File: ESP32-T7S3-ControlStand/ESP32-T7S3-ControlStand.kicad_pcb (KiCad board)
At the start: 2 copper layers, 199.4 x 126.4 mm, 188 parts, among them IC601 USBLC6-2SC6, J1 Button & LED Panel, J10 RJ45, J101 Keypad Panel, J11 Barrel_Jack, J12 Battery, J2 Button & LED Panel, J3 STEMMA (Display), J4 Horn, J5 Brake, J6 Light Switch, J601 GCT_USB4105, J7 Reverser, J8 Throttle, J9 RJ45, P1 CONN_8, P2 Misc buttons, bell, status LED, P6 CONN_3, P7 CONN_3, P701 CONN_5, P8 CONN_5, P9 CONN_5, SW1 A, SW10 SW_PUSH_SMALL, SW11 SW_PUSH_SMALL, SW12 SW_PUSH_SMALL, SW13 SW_PUSH_SMALL, SW14 SW_PUSH_SMALL, SW15 SW_PUSH_SMALL, SW16 SW_PUSH_SMALL, SW17 SW_PUSH_SMALL, SW18 SW_PUSH_SMALL, SW19 SW_PUSH_SMALL, SW2 B, SW20 SW_PUSH_SMALL, SW21 SW_PUSH_SMALL, SW22 SW_PUSH_SMALL, SW23 On/Off, SW24 RESET, SW3 C, SW4 D, SW5 Bell, SW601 BOOT, SW7 SW_PUSH_SMALL, SW701 "1", SW702 "4", SW703 "7", SW704 "*", SW705 "2", SW706 "5", SW707 "8", SW708 "0", SW709 "3", SW710 "6", SW711 "9", SW712 "#", SW8 SW_PUSH_SMALL, SW9 SW_PUSH_SMALL, T1 Buttons, T2 LEDS, T3 Buttons, T4 LEDS, T5 + 15 in -, T6 + 15 out -, U1 MCP23017, U2 TBD62083A, U3 MCP23017, U4 TBD62083A, U5 TCAN332DR, U6 MCP73871, U601 ESP32_S3_WROOM-1, U7 LM2574HVM-5.0, U701 TCA8418, U8 TC1263-3.3VOATR

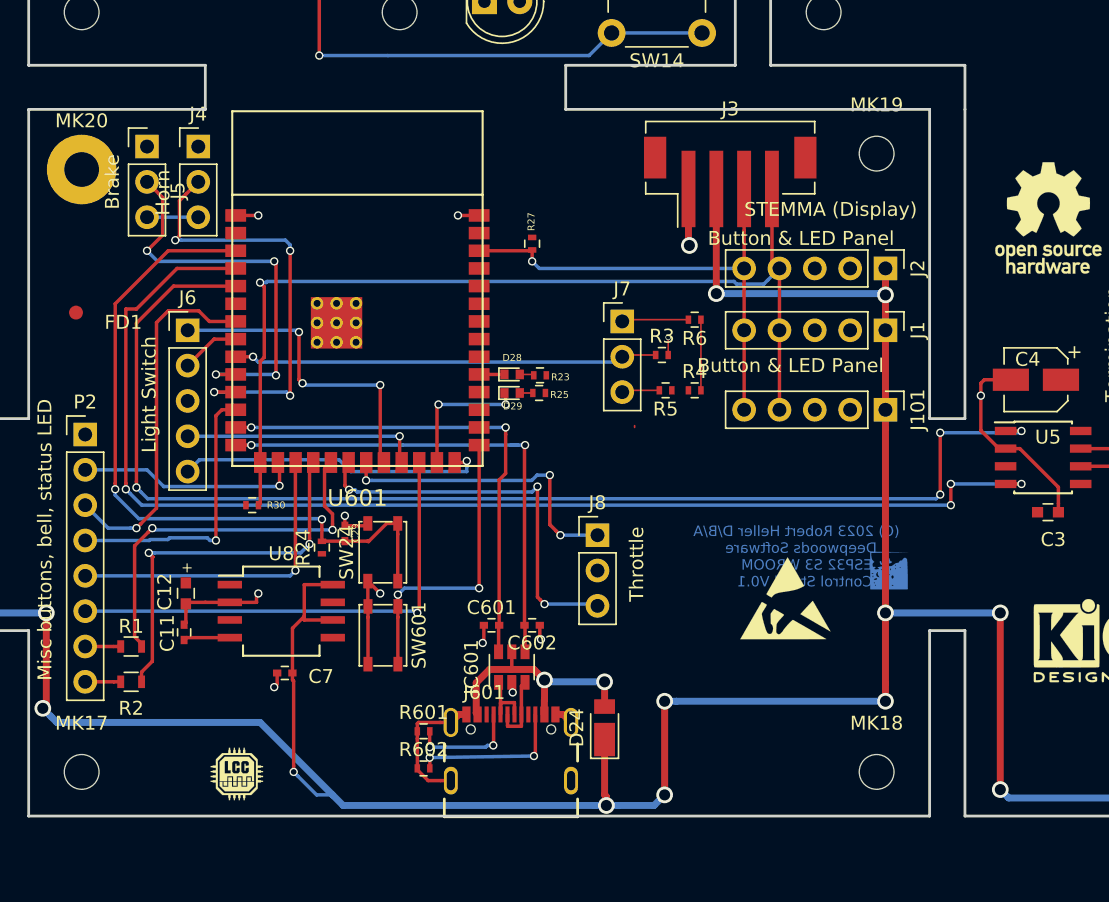
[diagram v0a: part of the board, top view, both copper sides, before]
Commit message: Add ESP32-T7S3-ControlStand.
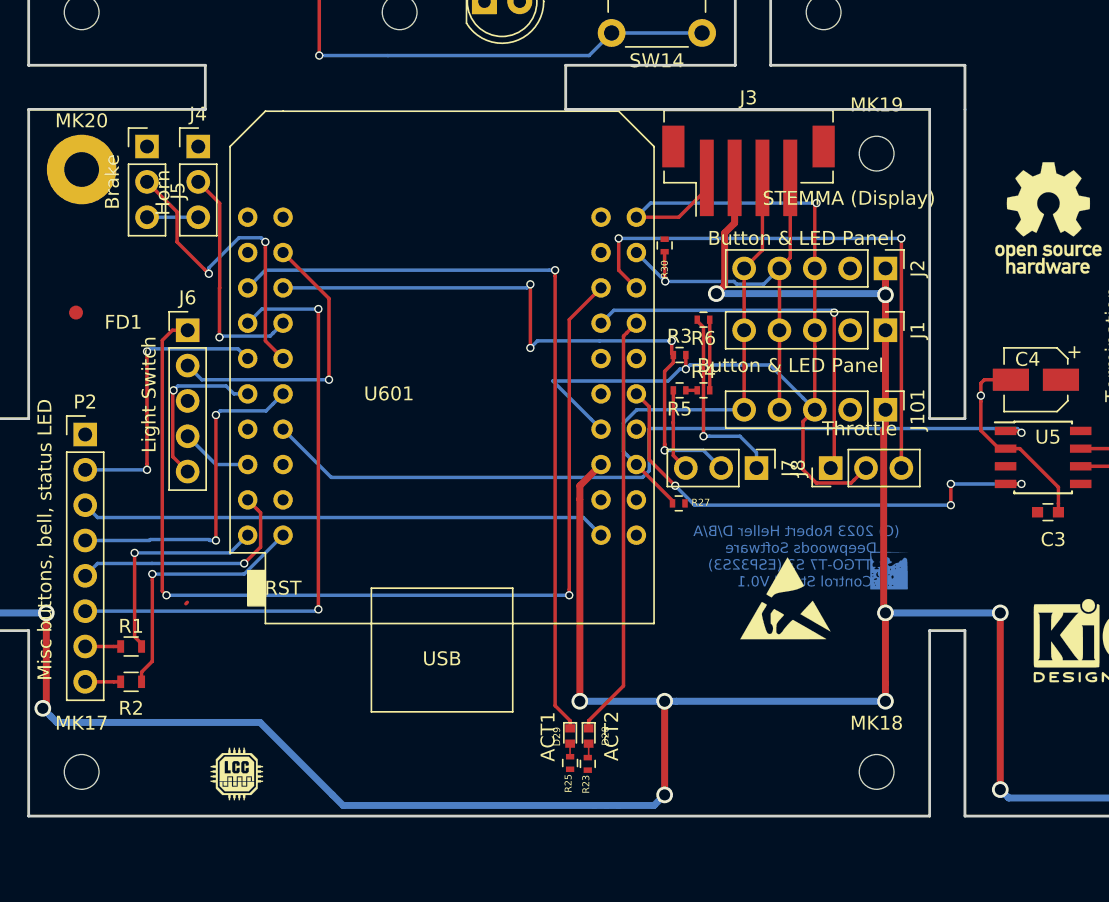
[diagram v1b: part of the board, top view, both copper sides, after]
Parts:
- removed C11: 470pf, Capacitors_SMD:C_0402
- removed C12: 1uf, MyCaps:C_0603_POL
- removed C29: 1uf, Capacitors_SMD:C_0402
- removed C601, C602: 22pf, Capacitors_SMD:C_0402
- removed C7: .1uf, Capacitors_SMD:C_0402
- removed D24: DFLS240-7, Diodes_SMD:D_PowerDI-123
- removed IC601: USBLC6-2SC6, TO_SOT_Packages_SMD:SOT-23-6
- removed J601: GCT_USB4105, GCT_USB:GCT_USB4105-GF-A
- removed R24: 10K, Resistors_SMD:R_0402
- removed R601, R602: 5.1K, Resistors_SMD:R_0402
- removed SW24: RESET, Buttons_Switches_SMD:SW_SPST_PTS810
- removed SW601: BOOT, Buttons_Switches_SMD:SW_SPST_PTS810
- removed U8: TC1263-3.3VOATR, Housings_SOIC:SO-8_5.3x6.2mm_Pitch1.27mm
- U601: value ESP32_S3_WROOM-1 -> TTGO-T7_S3-V1.1; footprint ESP32-WROOM:ESP32_S3_WROOM-1 -> ESP32_mini:ESP32_mini
- moved R30 35.0 mm to (158.8, 110.7), turned to 90 degrees
- moved R23 28.1 mm to (153.2, 148.0), turned to 90 degrees
- moved R25 26.7 mm to (152.0, 147.9), turned to 90 degrees
- moved D28 26.6 mm to (153.3, 146.0), turned to 270 degrees
- moved D29 25.0 mm to (152.0, 146.0), turned to 270 degrees
- moved R27 21.4 mm to (159.8, 129.3), turned to 180 degrees
- moved J8 17.4 mm to (170.7, 126.7), turned to 90 degrees
- moved J7 14.3 mm to (165.4, 126.7), turned to 270 degrees
- moved U601 6.64 mm to (142.7, 120.1)
- moved J3 1.54 mm to (164.8, 104.8)
- moved R3 1.27 mm to (159.8, 118.6)
- moved R5 1.01 mm to (159.8, 121.2)
- moved R4 0.64 mm to (161.5, 121.2)
- moved R6 0.64 mm to (161.5, 116.1)
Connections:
- MK20 pad 1: Net-(MK20-Pad1) -> GND
- R30 pad 2: +3V3 -> Net-(R30-Pad2)
- U601 pad 11: /Horn -> /L_Ditch
- U601 pad 13: /Processor Section/D- -> Net-(U601-Pad13)
- U601 pad 14: /Processor Section/D+ -> /CAN_TX
- U601 pad 15: /SCL -> /L_Bright
- U601 pad 16: /Button_A -> +3V3
- U601 pad 18: /Status_R -> Net-(U601-Pad18)
- U601 pad 2: +3V3 -> /RST
- U601 pad 20: /ThrottleA -> /Status_R
- U601 pad 21: /ThrottleB -> Net-(U601-Pad21)
- U601 pad 22: /L_Off -> GND
- U601 pad 23: /L_Bright -> Net-(U601-Pad23)
- U601 pad 24: /Bell -> /SCL
- U601 pad 25: /Processor Section/IO48(Act1) -> /L_Off
- U601 pad 26: /L_Ditch -> /ThrottleA
- U601 pad 27: Net-(SW601-Pad1) -> /ThrottleB
- U601 pad 28: Net-(U601-Pad28) -> /Processor Section/IO38(Act2)
- U601 pad 3: /RST -> Net-(U601-Pad3)
- U601 pad 31: /Processor Section/IO38(Act2) -> Net-(U601-Pad31)
- U601 pad 32: Net-(U601-Pad32) -> /CAN_RX
- U601 pad 33: Net-(U601-Pad33) -> GND
- U601 pad 35: Net-(U601-Pad35) -> +5V
- U601 pad 36: Net-(U601-Pad36) -> /SDA
- U601 pad 38: /SDA -> Net-(U601-Pad38)
- U601 pad 39: Net-(U601-Pad39) -> /Button_B
- U601 pad 4: /CAN_RX -> /L_Dim
- U601 pad 40: GND -> Net-(U601-Pad40)
- U601 pad 5: /CAN_TX -> /Processor Section/IO48(Act1)
- U601 pad 6: Net-(U601-Pad6) -> /Reverser
- U601 pad 7: /Button_B -> /Bell
- U601 pad 8: /L_Dim -> /Horn
- U601 pad 9: /Reverser -> /Button_A
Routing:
- net /CAN_RX: track 90.1 -> 36.4 mm
- net /RST: track 51.3 -> 0.00 mm, vias 2 -> 0
- net /L_Off: track 23.2 -> 72.6 mm, vias 3 -> 2
- net /Processor Section/IO48(Act1): track 9.90 -> 56.0 mm, vias 2 -> 1
- net /SCL: track 70.3 -> 31.6 mm
- net /Processor Section/D+: track 36.3 -> 0.00 mm, vias 2 -> 0
- net /Processor Section/D-: track 35.7 -> 0.00 mm, vias 2 -> 0
- net /CAN_TX: track 90.3 -> 59.6 mm, vias 4 -> 1
- net GND: track 279.0 -> 309.0 mm, vias 56 -> 47
- net /Processor Section/IO38(Act2): track 1.82 -> 30.5 mm
- net Net-(SW601-Pad1): track 21.3 -> 0.00 mm, vias 2 -> 0
- net VBUS: track 17.9 -> 0.00 mm, vias 2 -> 0
- net /L_Dim: track 4.24 -> 21.1 mm, vias 0 -> 1
- net /Reverser: track 30.4 -> 46.1 mm, vias 1 -> 4
- net /Horn: track 31.4 -> 17.0 mm, vias 4 -> 1
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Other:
- board text added: "(C) 2023 Robert Heller D/B/A Deepwoods Software TTGO-T7 S3 (ESP32S3) Control Stand V0.1"
- board text removed: "(C) 2023 Robert Heller D/B/A Deepwoods Software ESP32 S3 WROOM Control Stand V0.1"

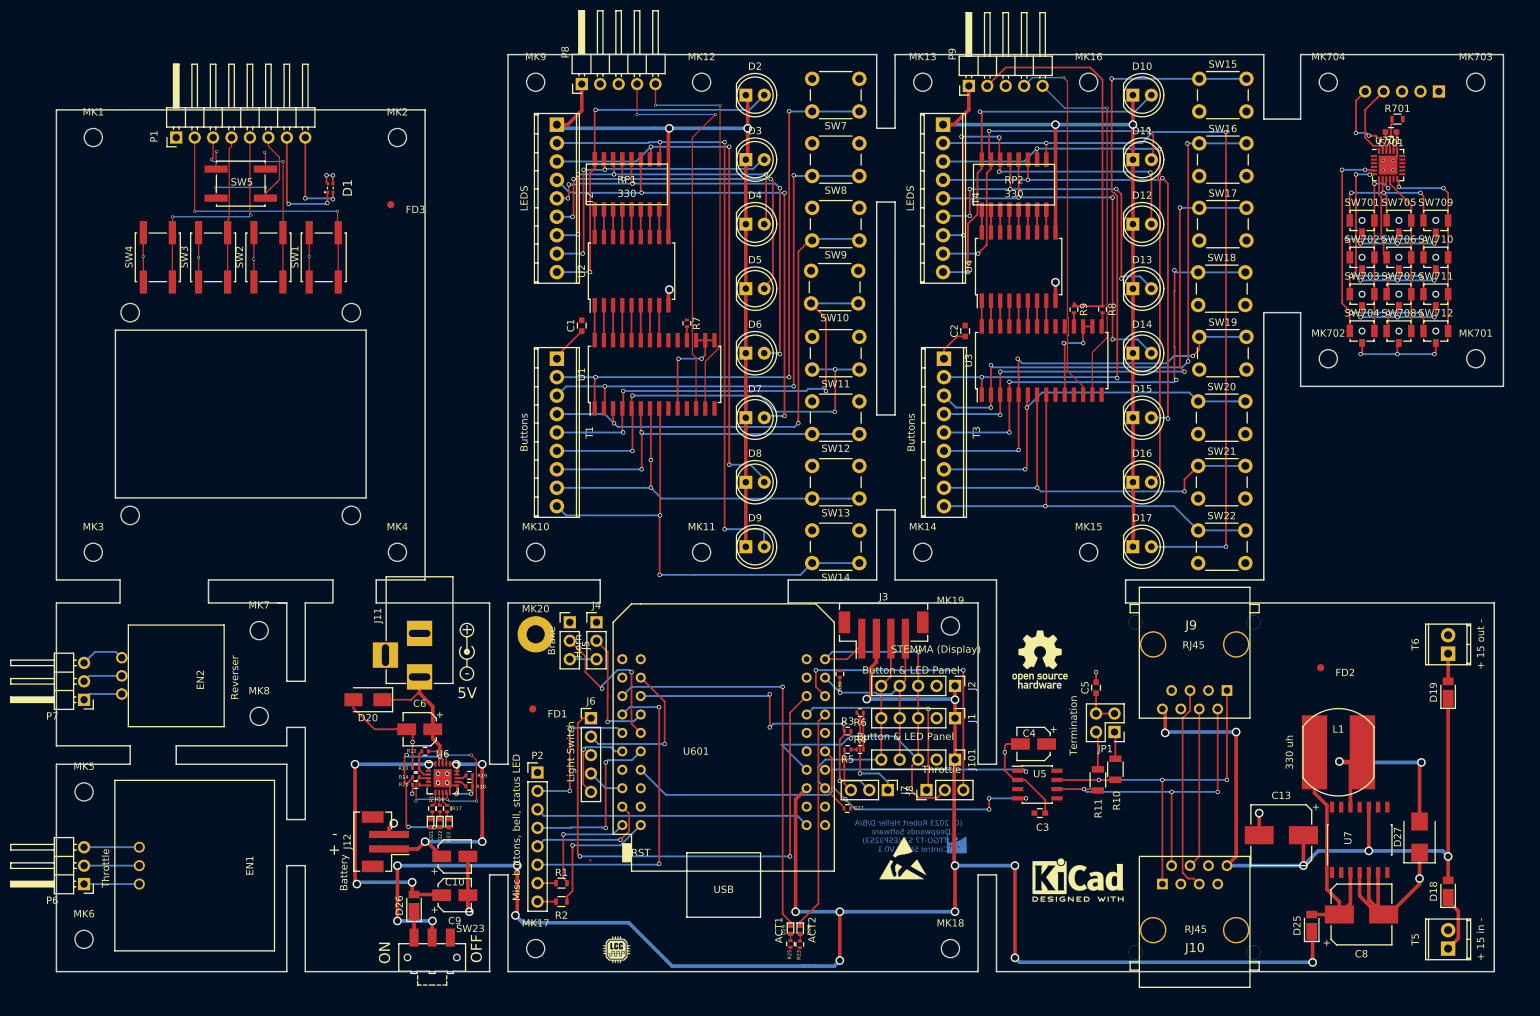
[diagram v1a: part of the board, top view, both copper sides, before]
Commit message: update ESP32-T7S3-ControlStand: Kicad 6, fix SDA, clean up and finalize PCB.
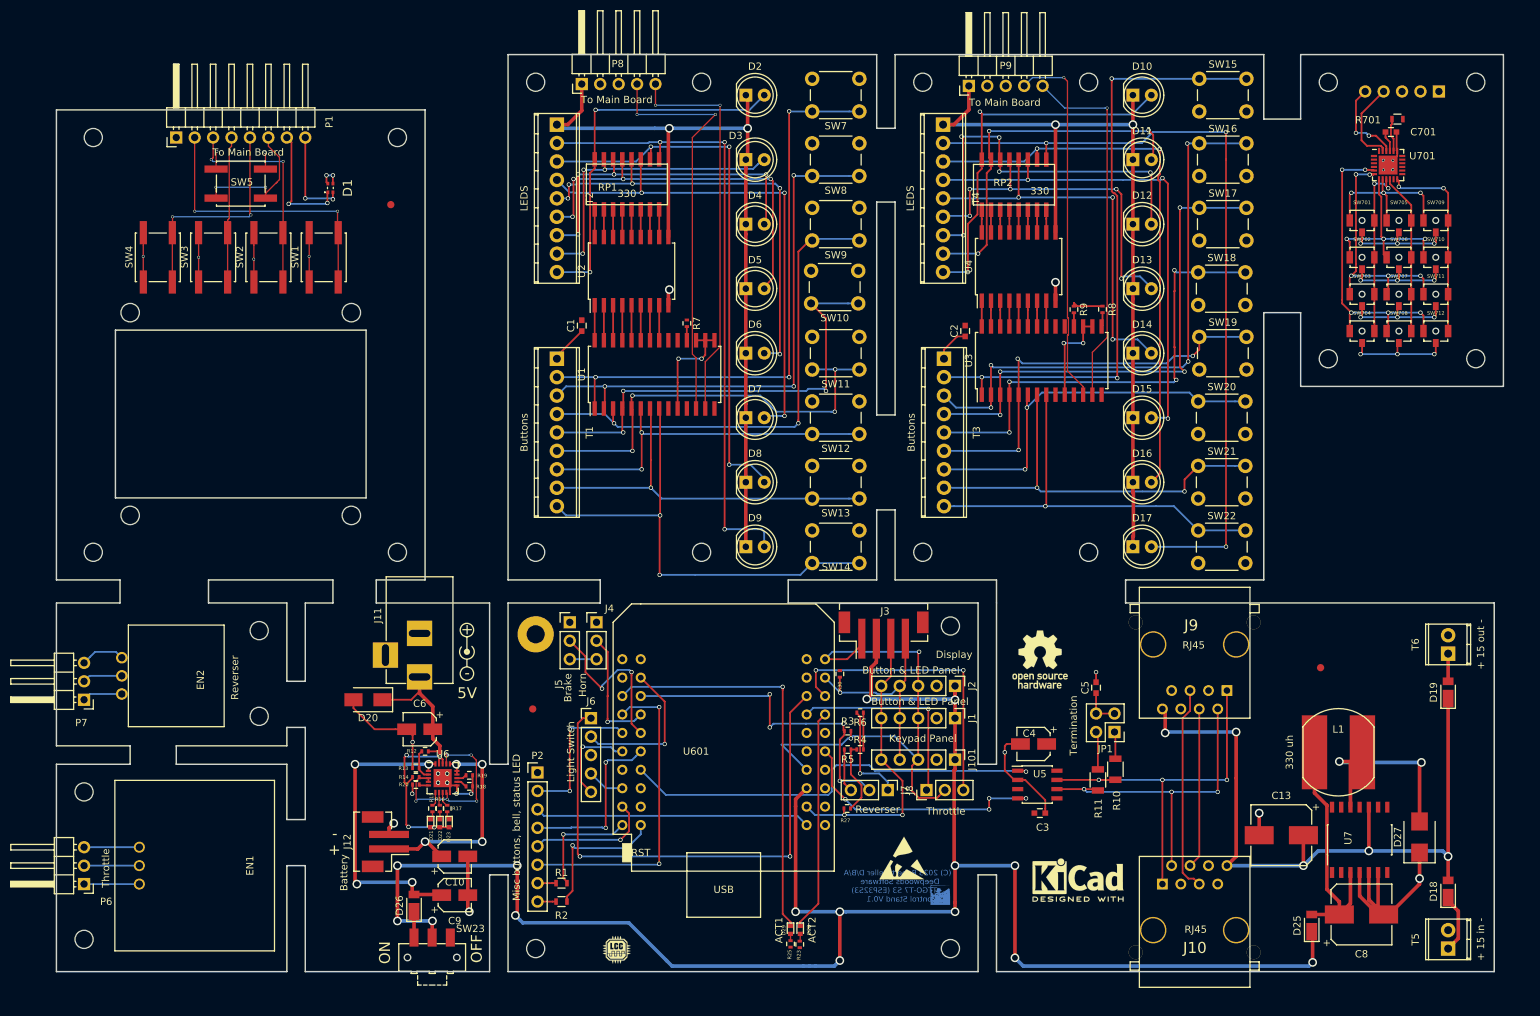
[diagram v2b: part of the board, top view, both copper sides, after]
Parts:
- J3: value STEMMA (Display) -> Display
- P1: value CONN_8 -> To Main Board
- P6, P7: value CONN_3 -> To Main Board
- P701, P8, P9: value CONN_5 -> To Main Board
- moved ? 7.47 mm to (172.6, 141.2)
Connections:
- J11 pad 3: Net-(J11-Pad3) -> unconnected-(J11-Pad3)
- P701 pad 1: Net-(P701-Pad1) -> unconnected-(P701-Pad1)
- R30 pad 2: Net-(R30-Pad2) -> unconnected-(R30-Pad2)
- SW23 pad 3: Net-(SW23-Pad3) -> unconnected-(SW23-Pad3)
- U1 pad 19: Net-(U1-Pad19) -> unconnected-(U1-Pad19)
- U1 pad 20: Net-(U1-Pad20) -> unconnected-(U1-Pad20)
- U3 pad 19: Net-(U3-Pad19) -> unconnected-(U3-Pad19)
- U3 pad 20: Net-(U3-Pad20) -> unconnected-(U3-Pad20)
- U5 pad 5: Net-(U5-Pad5) -> unconnected-(U5-Pad5)
- U5 pad 8: Net-(U5-Pad8) -> unconnected-(U5-Pad8)
- U601 pad 13: Net-(U601-Pad13) -> unconnected-(U601-Pad13)
- U601 pad 18: Net-(U601-Pad18) -> unconnected-(U601-Pad18)
- U601 pad 21: Net-(U601-Pad21) -> unconnected-(U601-Pad21)
- U601 pad 23: Net-(U601-Pad23) -> unconnected-(U601-Pad23)
- U601 pad 29: Net-(U601-Pad29) -> unconnected-(U601-Pad29)
- U601 pad 3: Net-(U601-Pad3) -> unconnected-(U601-Pad3)
- U601 pad 30: Net-(U601-Pad30) -> unconnected-(U601-Pad30)
- U601 pad 31: Net-(U601-Pad31) -> unconnected-(U601-Pad31)
- U601 pad 34: Net-(U601-Pad34) -> unconnected-(U601-Pad34)
- U601 pad 36: /SDA -> unconnected-(U601-Pad36)
- U601 pad 37: Net-(U601-Pad37) -> /SDA
- U601 pad 38: Net-(U601-Pad38) -> unconnected-(U601-Pad38)
- U601 pad 40: Net-(U601-Pad40) -> unconnected-(U601-Pad40)
- U7 pad 1: Net-(U7-Pad1) -> unconnected-(U7-Pad1)
- U7 pad 11: Net-(U7-Pad11) -> unconnected-(U7-Pad11)
- U7 pad 13: Net-(U7-Pad13) -> unconnected-(U7-Pad13)
- U7 pad 14: Net-(U7-Pad14) -> unconnected-(U7-Pad14)
- U7 pad 2: Net-(U7-Pad2) -> unconnected-(U7-Pad2)
- U7 pad 7: Net-(U7-Pad7) -> unconnected-(U7-Pad7)
- U7 pad 8: Net-(U7-Pad8) -> unconnected-(U7-Pad8)
- U7 pad 9: Net-(U7-Pad9) -> unconnected-(U7-Pad9)
- U701 pad 1: Net-(U701-Pad1) -> unconnected-(U701-Pad1)
- U701 pad 13: Net-(U701-Pad13) -> unconnected-(U701-Pad13)
- U701 pad 14: Net-(U701-Pad14) -> unconnected-(U701-Pad14)
- U701 pad 15: Net-(U701-Pad15) -> unconnected-(U701-Pad15)
- U701 pad 16: Net-(U701-Pad16) -> unconnected-(U701-Pad16)
- U701 pad 17: Net-(U701-Pad17) -> unconnected-(U701-Pad17)
- U701 pad 18: Net-(U701-Pad18) -> unconnected-(U701-Pad18)
- U701 pad 2: Net-(U701-Pad2) -> unconnected-(U701-Pad2)
- U701 pad 24: Net-(U701-Pad24) -> unconnected-(U701-Pad24)
- U701 pad 3: Net-(U701-Pad3) -> unconnected-(U701-Pad3)
- U701 pad 4: Net-(U701-Pad4) -> unconnected-(U701-Pad4)
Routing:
- net +3V3: track 57.3 -> 17.6 mm
- net /SDA: track 33.5 -> 40.6 mm, vias 0 -> 2
- net Net-(D17-Pad2): track 111.1 -> 109.3 mm
- net Net-(SW21-Pad1): track 58.4 -> 57.0 mm
- net Net-(C10-Pad1): track 34.2 -> 33.0 mm
- net /Status_R: track 18.6 -> 19.7 mm
- net /Keypad Panel/SCL: track 10.9 -> 11.8 mm
- net /SCL: track 31.6 -> 30.8 mm
- net /L_Ditch: track 12.0 -> 12.6 mm
- net /CAN_RX: track 36.4 -> 35.9 mm
- net Net-(D8-Pad2): track 76.3 -> 75.8 mm
- net GND: track 309.0 -> 308.7 mm, vias 47 -> 46
- net Net-(SW13-Pad1): vias 2 -> 1
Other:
- outline, holes or cut-outs redrawn
- net class Default removed
